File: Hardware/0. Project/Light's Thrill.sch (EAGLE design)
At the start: 39 parts, among them CN1 Micro-USB, CN2 2.1MMJACKTHM, Q1 SI2302DS, Q2 SI2302DS, Q3 SI2302DS, U1 TSOP1838, U2 ATMEGA32U4, U3 LM1117-5.0, Y1 16 MHz

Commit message: PCB Layout 1.2 - DONE
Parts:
- R1, R10, R11, R12, R13, R2, R3, R4, R5, R6, R7, R8, R9: device rcl:R-EU_M0805 -> rcl:R-EU_R0805
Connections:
- net 12V_DETECT: now also U2.PB4(ADC11); no longer U2.PD1(INT1/SDA)
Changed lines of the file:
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@@
 <parts>
 <part name="FRAME1" library="frames-OSHW" deviceset="DINA4_L" device=""/>
-<part name="Q1" library="SI2302DS" deviceset="SI2302DS" device=""/>
-<part name="U2" library="adafruit" deviceset="ATMEGA32U4" device="-AU" package3d_urn="urn:adsk.eagle:package:6240644/1" value="ATMEGA32U4"/>
-<part name="R4" library="rcl" deviceset="R-EU_" device="M0805" value="1k (5%)"/>
+<part name="Q1" library="SI2302DS" deviceset="SI2302DS" device="" package3d_urn="urn:adsk.eagle:package:21787272/2"/>
+<part name="U2" library="adafruit" deviceset="ATMEGA32U4" device="-AU" package3d_urn="urn:adsk.eagle:package:6240644/1" override_package3d_urn="urn:adsk.eagle:package:21786985/2" override_package_urn="urn:adsk.eagle:footprint:6239998/1" value="ATMEGA32U4"/>
+<part name="R4" library="rcl" library_urn="urn:adsk.eagle:library:334" deviceset="R-EU_" device="R0805" package3d_urn="urn:adsk.eagle:package:23553/2" value="1k (5%)"/>
 <part name="GND1" library="supply1" deviceset="GND" device=""/>
-<part name="Q2" library="SI2302DS" deviceset="SI2302DS" device=""/>
-<part name="R7" library="rcl" deviceset="R-EU_" device="M0805" value="1k (5%)"/>
+<part name="Q2" library="SI2302DS" deviceset="SI2302DS" device="" package3d_urn="urn:adsk.eagle:package:21787272/2"/>
+<part name="R7" library="rcl" library_urn="urn:adsk.eagle:library:334" deviceset="R-EU_" device="R0805" package3d_urn="urn:adsk.eagle:package:23553/2" value="1k (5%)"/>
 <part name="GND2" library="supply1" deviceset="GND" device=""/>
-<part name="Q3" library="SI2302DS" deviceset="SI2302DS" device=""/>
-<part name="R13" library="rcl" deviceset="R-EU_" device="M0805" value="1k (5%)"/>
+<part name="Q3" library="SI2302DS" deviceset="SI2302DS" device="" package3d_urn="urn:adsk.eagle:package:21787272/2"/>
+<part name="R13" library="rcl" library_urn="urn:adsk.eagle:library:334" deviceset="R-EU_" device="R0805" package3d_urn="urn:adsk.eagle:package:23553/2" value="1k (5%)"/>
 <part name="GND3" library="supply1" deviceset="GND" device=""/>
-<part name="LED1" library="led" deviceset="RGB_LED_STRIP" device=""/>
+<part name="LED1" library="led" deviceset="RGB_LED_STRIP" device="" override_package3d_urn="urn:adsk.eagle:package:21787266/2" override_package_urn="urn:adsk.eagle:footprint:21787267/1"/>
 <part name="SUPPLY4" library="supply2" library_urn="urn:adsk.eagle:library:372" deviceset="+5V" device=""/>
-<part name="R2" library="rcl" deviceset="R-EU_" device="M0805" value="10k (5%)"/>
+<part name="R2" library="rcl" library_urn="urn:adsk.eagle:library:334" deviceset="R-EU_" device="R0805" package3d_urn="urn:adsk.eagle:package:23553/2" value="10k (5%)"/>
 <part name="SUPPLY5" library="supply2" library_urn="urn:adsk.eagle:library:372" deviceset="+5V" device=""/>
 <part name="GND4" library="supply1" deviceset="GND" device=""/>
 <part name="SUPPLY6" library="supply2" library_urn="urn:adsk.eagle:library:372" deviceset="+5V" device=""/>
-<part name="R3" library="rcl" deviceset="R-EU_" device="M0805" value="100R (5%)"/>
+<part name="R3" library="rcl" library_urn="urn:adsk.eagle:library:334" deviceset="R-EU_" device="R0805" package3d_urn="urn:adsk.eagle:package:23553/2" value="100R (5%)"/>
 <part name="C3" library="rcl" library_urn="urn:adsk.eagle:library:334" deviceset="CPOL-EU" device="E2-5" package3d_urn="urn:adsk.eagle:package:23346/2" value="100uF x 16V"/>
 <part name="GND5" library="supply1" deviceset="GND" device=""/>
 <part name="GND6" library="supply1" deviceset="GND" device=""/>
-<part name="R5" library="rcl" deviceset="R-EU_" device="M0805" value="22R (5%)"/>
-<part name="R6" library="rcl" deviceset="R-EU_" device="M0805" value="22R (5%)"/>
+<part name="R5" library="rcl" library_urn="urn:adsk.eagle:library:334" deviceset="R-EU_" device="R0805" package3d_urn="urn:adsk.eagle:package:23553/2" value="22R (5%)"/>
+<part name="R6" library="rcl" library_urn="urn:adsk.eagle:library:334" deviceset="R-EU_" device="R0805" package3d_urn="urn:adsk.eagle:package:23553/2" value="22R (5%)"/>
 <part name="SUPPLY7" library="supply2" library_urn="urn:adsk.eagle:library:372" deviceset="+5V" device=""/>
-<part name="R1" library="rcl" deviceset="R-EU_" device="M0805" value="10k (5%)"/>
+<part name="R1" library="rcl" library_urn="urn:adsk.eagle:library:334" deviceset="R-EU_" device="R0805" package3d_urn="urn:adsk.eagle:package:23553/2" value="10k (5%)"/>
 <part name="SUPPLY8" library="supply2" library_urn="urn:adsk.eagle:library:372" deviceset="+5V" device=""/>
 <part name="C6" library="rcl" library_urn="urn:adsk.eagle:library:334" deviceset="C-EU" device="C0805" package3d_urn="urn:adsk.eagle:package:23617/2" value="1uF x 50V"/>
@@
 <part name="C7" library="rcl" library_urn="urn:adsk.eagle:library:334" deviceset="C-EU" device="C0805" package3d_urn="urn:adsk.eagle:package:23617/2" value="100nF x 50V"/>
 <part name="GND9" library="supply1" deviceset="GND" device=""/>
-<part name="Y1" library="crystal-geyer_V1_0" deviceset="KX" device="-9A" package3d_urn="urn:adsk.eagle:package:11927/1" value="16 MHz"/>
+<part name="Y1" library="crystal-geyer_V1_0" deviceset="KX" device="-9A" package3d_urn="urn:adsk.eagle:package:11927/1" override_package3d_urn="urn:adsk.eagle:package:21787413/2" override_package_urn="urn:adsk.eagle:footprint:11874/1" value="16 MHz"/>
 <part name="C4" library="rcl" library_urn="urn:adsk.eagle:library:334" deviceset="C-EU" device="C0805" package3d_urn="urn:adsk.eagle:package:23617/2" value="1uF x 50V"/>
 <part name="C5" library="rcl" library_urn="urn:adsk.eagle:library:334" deviceset="C-EU" device="C0805" package3d_urn="urn:adsk.eagle:package:23617/2" value="1uF x 50V"/>
@@
 <part name="GND15" library="supply1" deviceset="GND" device=""/>
 <part name="D3" library="diode" deviceset="CGRM400*-G" device="" package3d_urn="urn:adsk.eagle:package:43457/2" technology="7" value="US1A"/>
-<part name="U3" library="LM1117IMP-5.0-NOPB" deviceset="LM1117IMP-5.0-NOPB" device="" value="LM1117-5.0"/>
+<part name="U3" library="LM1117IMP-5.0-NOPB" deviceset="LM1117IMP-5.0-NOPB" device="" override_package3d_urn="urn:adsk.eagle:package:21787392/2" override_package_urn="urn:adsk.eagle:footprint:21787393/1" value="LM1117-5.0"/>
 <part name="C8" library="rcl" library_urn="urn:adsk.eagle:library:334" deviceset="C-EU" device="C0805" package3d_urn="urn:adsk.eagle:package:23617/2" value="100nF x 50V"/>
 <part name="C9" library="rcl" library_urn="urn:adsk.eagle:library:334" deviceset="C-EU" device="C0805" package3d_urn="urn:adsk.eagle:package:23617/2" value="1uF x 50V"/>
@@
 <part name="GND16" library="supply1" deviceset="GND" device=""/>
 <part name="LED2" library="led" deviceset="LED" device="CHIPLED_0805" package3d_urn="urn:adsk.eagle:package:15821/2"/>
-<part name="S1" library="switch-tact2" deviceset="DTSM-3" device="" value=""/>
-<part name="R10" library="rcl" deviceset="R-EU_" device="M0805" value="10k (5%)"/>
+<part name="S1" library="switch-tact2" deviceset="DTSM-3" device="" override_package3d_urn="urn:adsk.eagle:package:21787057/2" override_package_urn="urn:adsk.eagle:footprint:21787059/1" value=""/>
+<part name="R10" library="rcl" library_urn="urn:adsk.eagle:library:334" deviceset="R-EU_" device="R0805" package3d_urn="urn:adsk.eagle:package:23553/2" value="10k (5%)"/>
 <part name="SUPPLY1" library="supply2" library_urn="urn:adsk.eagle:library:372" deviceset="+5V" device=""/>
 <part name="GND14" library="supply1" deviceset="GND" device=""/>
-<part name="R11" library="rcl" deviceset="R-EU_" device="M0805" value="100R (5%)"/>
+<part name="R11" library="rcl" library_urn="urn:adsk.eagle:library:334" deviceset="R-EU_" device="R0805" package3d_urn="urn:adsk.eagle:package:23553/2" value="100R (5%)"/>
 <part name="C11" library="rcl" library_urn="urn:adsk.eagle:library:334" deviceset="C-EU" device="C0805" package3d_urn="urn:adsk.eagle:package:23617/2" value="100nF x 50V"/>
 <part name="GND17" library="supply1" deviceset="GND" device=""/>
-<part name="R12" library="rcl" deviceset="R-EU_" device="M0805" value="100R (5%)"/>
+<part name="R12" library="rcl" library_urn="urn:adsk.eagle:library:334" deviceset="R-EU_" device="R0805" package3d_urn="urn:adsk.eagle:package:23553/2" value="100R (5%)"/>
 <part name="GND18" library="supply1" deviceset="GND" device=""/>
-<part name="R8" library="rcl" deviceset="R-EU_" device="M0805" value="220k (5%)"/>
-<part name="R9" library="rcl" deviceset="R-EU_" device="M0805" value="100k (5%)"/>
+<part name="R8" library="rcl" library_urn="urn:adsk.eagle:library:334" deviceset="R-EU_" device="R0805" package3d_urn="urn:adsk.eagle:package:23553/2" value="220k (5%)"/>
+<part name="R9" library="rcl" library_urn="urn:adsk.eagle:library:334" deviceset="R-EU_" device="R0805" package3d_urn="urn:adsk.eagle:package:23553/2" value="100k (5%)"/>
 <part name="SUPPLY12" library="supply2" library_urn="urn:adsk.eagle:library:372" deviceset="+12V" device=""/>
 <part name="GND19" library="supply1" deviceset="GND" device=""/>
@@
 </instance>
 <instance part="D2" gate="G$1" x="126.365" y="63.5" smashed="yes" rot="R180" grouprefs="EXTERNAL_POWER_SUPPLY">
-<attribute name="NAME" x="127.889" y="61.4934" size="1.778" layer="95" rot="R180"/>
-<attribute name="VALUE" x="128.651" y="66.5734" size="1.27" layer="96" rot="R180"/>
+<attribute name="NAME" x="124.714" y="65.7606" size="1.778" layer="95"/>
+<attribute name="VALUE" x="124.333" y="60.1726" size="1.27" layer="96"/>
 </instance>
 <instance part="SUPPLY11" gate="+5V" x="116.84" y="67.945" smashed="yes" grouprefs="EXTERNAL_POWER_SUPPLY">
@@
 </segment>
 <segment>
-<pinref part="U2" gate="G$1" pin="PD1(INT1/SDA)"/>
-<wire x1="169.545" y1="88.9" x2="173.355" y2="88.9" width="0.1524" layer="91"/>
-<label x="173.355" y="88.9" size="1.27" layer="95" xref="yes"/>
-</segment>
-</net>
+<label x="173.355" y="119.38" size="1.27" layer="95" xref="yes"/>
+<pinref part="U2" gate="G$1" pin="PB4(ADC11)"/>
+<wire x1="169.545" y1="119.38" x2="173.355" y2="119.38" width="0.1524" layer="91"/>
+</segment>
+</net>

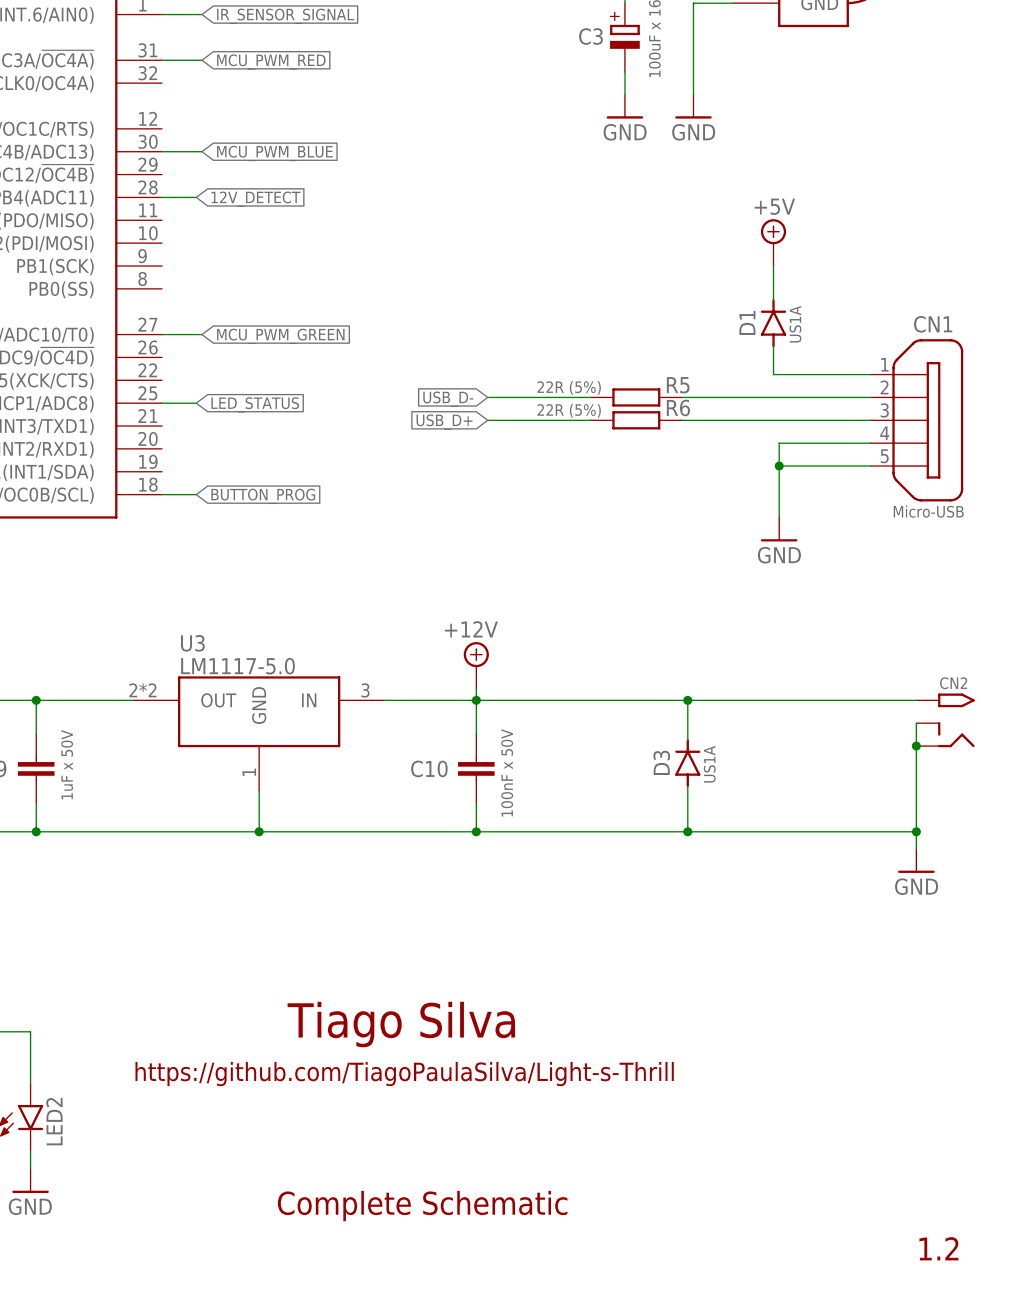
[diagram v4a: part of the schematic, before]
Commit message: Schematic + PCB 1.3 up to date
- Change MCU_PWM_RED to a 16 bit PWM pin.
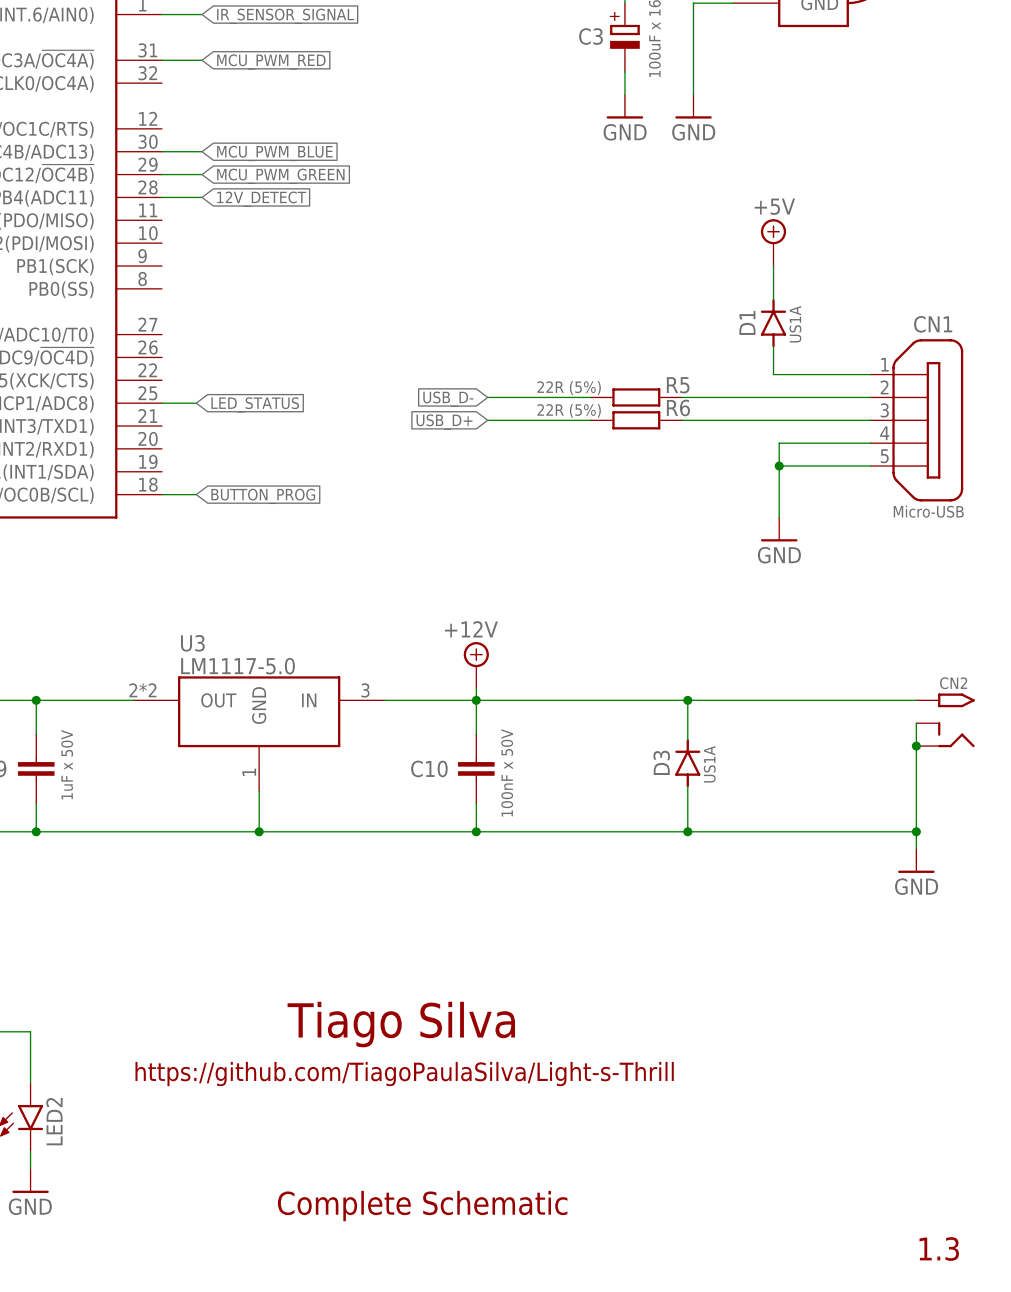
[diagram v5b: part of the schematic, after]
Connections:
- net MCU_PWM_GREEN: now also U2.PB5(OC1A/ADC12/!OC4B); no longer U2.PD7(OC4D/ADC10/T0)
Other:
- note added: "1.3"
- note added: "D9"
- note removed: "1.2"
- note removed: "D6"
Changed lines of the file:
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@@
 <layer number="96" name="Values" color="7" fill="1" visible="yes" active="yes"/>
 <layer number="97" name="Info" color="7" fill="1" visible="yes" active="yes"/>
-<layer number="98" name="Guide" color="6" fill="1" visible="no" active="yes"/>
+<layer number="98" name="Guide" color="6" fill="1" visible="yes" active="yes"/>
 <layer number="99" name="SpiceOrder" color="5" fill="1" visible="no" active="yes"/>
 <layer number="100" name="Muster" color="7" fill="1" visible="no" active="no"/>
@@
 <text x="183.515" y="26.035" size="3.81" layer="94">Tiago Silva</text>
 <text x="166.37" y="21.209" size="2.032" layer="94">https://github.com/TiagoPaulaSilva/Light-s-Thrill</text>
-<text x="253.365" y="1.27" size="2.54" layer="94" ratio="5">1.2</text>
+<text x="253.365" y="1.27" size="2.54" layer="94" ratio="5">1.3</text>
 <text x="182.245" y="6.35" size="2.54" layer="94" ratio="5">Complete Schematic</text>
 <wire x1="46.99" y1="97.79" x2="46.99" y2="100.33" width="0.1524" layer="94" grouprefs="RGB_LED_STRIP"/>
@@
 <text x="32.385" y="58.42" size="2.54" layer="213" font="vector" ratio="12" align="center" grouprefs="RGB_LED_STRIP">BLUE</text>
 <text x="171.45" y="135.89" size="1.27" layer="98" font="vector" align="center" grouprefs="MICROCONTROLLER">D5</text>
-<text x="171.45" y="105.41" size="1.27" layer="98" font="vector" align="center" grouprefs="MICROCONTROLLER">D6</text>
+<text x="171.45" y="123.19" size="1.27" layer="98" font="vector" align="center" grouprefs="MICROCONTROLLER">D9</text>
 <text x="171.45" y="125.73" size="1.27" layer="98" font="vector" align="center" grouprefs="MICROCONTROLLER">D10</text>
 <text x="171.45" y="140.97" size="1.27" layer="98" font="vector" align="center" grouprefs="MICROCONTROLLER">D7</text>
@@
 <net name="MCU_PWM_GREEN" class="0">
 <segment>
-<label x="173.99" y="104.14" size="1.27" layer="95" font="vector" xref="yes" grouprefs="MICROCONTROLLER"/>
-<pinref part="U2" gate="G$1" pin="PD7(OC4D/ADC10/T0)"/>
-<wire x1="169.545" y1="104.14" x2="173.99" y2="104.14" width="0.1524" layer="91" grouprefs="MICROCONTROLLER"/>
+<label x="173.99" y="121.92" size="1.27" layer="95" font="vector" xref="yes" grouprefs="MICROCONTROLLER"/>
+<pinref part="U2" gate="G$1" pin="PB5(OC1A/ADC12/!OC4B)"/>
+<wire x1="169.545" y1="121.92" x2="173.99" y2="121.92" width="0.1524" layer="91"/>
 </segment>
 <segment>
@@
 </segment>
 <segment>
-<label x="173.355" y="119.38" size="1.27" layer="95" xref="yes"/>
+<label x="173.99" y="119.38" size="1.27" layer="95" xref="yes"/>
 <pinref part="U2" gate="G$1" pin="PB4(ADC11)"/>
-<wire x1="169.545" y1="119.38" x2="173.355" y2="119.38" width="0.1524" layer="91"/>
-</segment>
-</net>
+<wire x1="169.545" y1="119.38" x2="173.99" y2="119.38" width="0.1524" layer="91"/>
+</segment>
+</net>
